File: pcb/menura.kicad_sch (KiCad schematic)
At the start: 53 parts, among them SW1 SW_Push, SW10 SW_Push, SW11 SW_Push, SW12 SW_Push, SW13 SW_Push, SW14 SW_Push, SW15 SW_Push, SW16 SW_Push, SW17 SW_Push, SW18 SW_Push, SW19 SW_Push, SW2 SW_Push, SW20 SW_Push, SW21 SW_Push, SW22 SW_Push, SW3 SW_Push, SW4 SW_Push, SW5 SW_Push, SW6 SW_Push, SW7 SW_Push, SW8 SW_Push, SW9 SW_Push

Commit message: fix diode ordering
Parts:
- renumbered D20 to D19, D22 to D20, D19 to D21, D21 to D22, SW20 to SW19, SW22 to SW20, SW19 to SW21, SW21 to SW22
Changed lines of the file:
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@@
 		(on_board yes)
 		(dnp no)
-		(property "Reference" "D19"
+		(property "Reference" "D21"
 			(at 154.94 105.41 90)
 			(effects
@@
 			(project "menura"
 				(path "/e9ea61dd-32b8-44c9-bab5-2f724da397cf"
-					(reference "D19")
+					(reference "D21")
 					(unit 1)
 				)
@@
 		(on_board yes)
 		(dnp no)
-		(property "Reference" "D22"
+		(property "Reference" "D20"
 			(at 179.07 91.44 90)
 			(effects
@@
 			(project "menura"
 				(path "/e9ea61dd-32b8-44c9-bab5-2f724da397cf"
-					(reference "D22")
+					(reference "D20")
 					(unit 1)
 				)
@@
 		(on_board yes)
 		(dnp no)
-		(property "Reference" "SW22"
+		(property "Reference" "SW20"
 			(at 170.18 82.55 0)
 			(effects
@@
 			(project "menura"
 				(path "/e9ea61dd-32b8-44c9-bab5-2f724da397cf"
-					(reference "SW22")
+					(reference "SW20")
 					(unit 1)
 				)
@@
 		(on_board yes)
 		(dnp no)
-		(property "Reference" "D20"
+		(property "Reference" "D19"
 			(at 160.02 91.44 90)
 			(effects
@@
 			(project "menura"
 				(path "/e9ea61dd-32b8-44c9-bab5-2f724da397cf"
-					(reference "D20")
+					(reference "D19")
 					(unit 1)
 				)
@@
 		(on_board yes)
 		(dnp no)
-		(property "Reference" "SW19"
+		(property "Reference" "SW21"
 			(at 146.05 96.52 0)
 			(effects
@@
 			(project "menura"
 				(path "/e9ea61dd-32b8-44c9-bab5-2f724da397cf"
-					(reference "SW19")
+					(reference "SW21")
 					(unit 1)
 				)
@@
 		(on_board yes)
 		(dnp no)
-		(property "Reference" "SW20"
+		(property "Reference" "SW19"
 			(at 151.13 82.55 0)
 			(effects
@@
 			(project "menura"
 				(path "/e9ea61dd-32b8-44c9-bab5-2f724da397cf"
-					(reference "SW20")
+					(reference "SW19")
 					(unit 1)
 				)
@@
 		(on_board yes)
 		(dnp no)
-		(property "Reference" "D21"
+		(property "Reference" "D22"
 			(at 173.99 105.41 90)
 			(effects
@@
 			(project "menura"
 				(path "/e9ea61dd-32b8-44c9-bab5-2f724da397cf"
-					(reference "D21")
+					(reference "D22")
 					(unit 1)
 				)
@@
 		(on_board yes)
 		(dnp no)
-		(property "Reference" "SW21"
+		(property "Reference" "SW22"
 			(at 165.1 96.52 0)
 			(effects
@@
 			(project "menura"
 				(path "/e9ea61dd-32b8-44c9-bab5-2f724da397cf"
-					(reference "SW21")
+					(reference "SW22")
 					(unit 1)
 				)

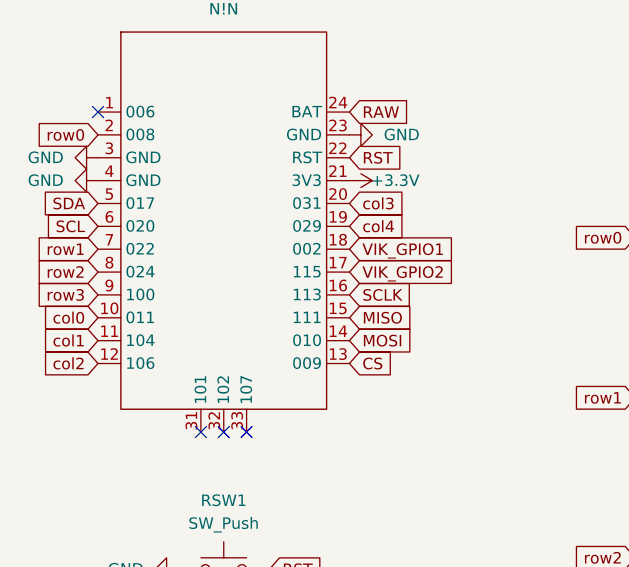
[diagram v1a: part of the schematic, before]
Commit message: fix: spi pins should be high freq
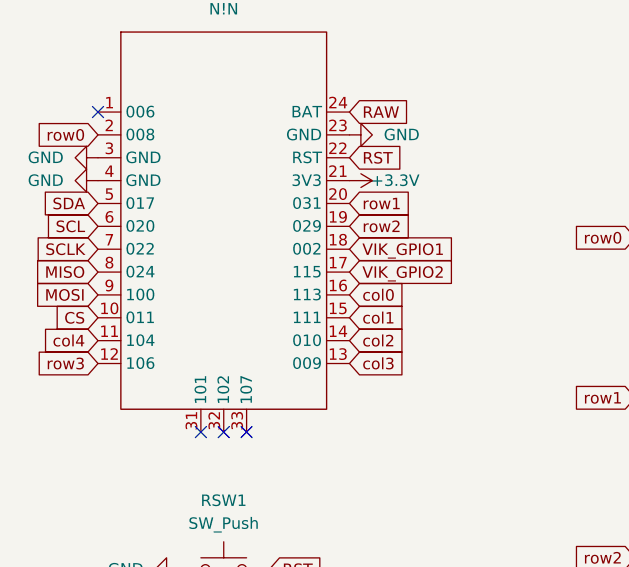
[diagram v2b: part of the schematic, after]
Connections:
- net CS: now also MCU1.10 (011); no longer MCU1.13 (009)
- net MISO: now also MCU1.8 (024); no longer MCU1.15 (111)
- net MOSI: now also MCU1.9 (100); no longer MCU1.14 (010)
- net SCLK: now also MCU1.7 (022); no longer MCU1.16 (113)
- net col0: now also MCU1.16 (113); no longer MCU1.10 (011)
- net col1: now also MCU1.15 (111); no longer MCU1.11 (104)
- net col2: now also MCU1.14 (010); no longer MCU1.12 (106)
- net col3: now also MCU1.13 (009); no longer MCU1.20 (031)
- net col4: now also MCU1.11 (104); no longer MCU1.19 (029)
- net row1: now also MCU1.20 (031); no longer MCU1.7 (022)
- net row2: now also MCU1.19 (029); no longer MCU1.8 (024)
- net row3: now also MCU1.12 (106); no longer MCU1.9 (100)

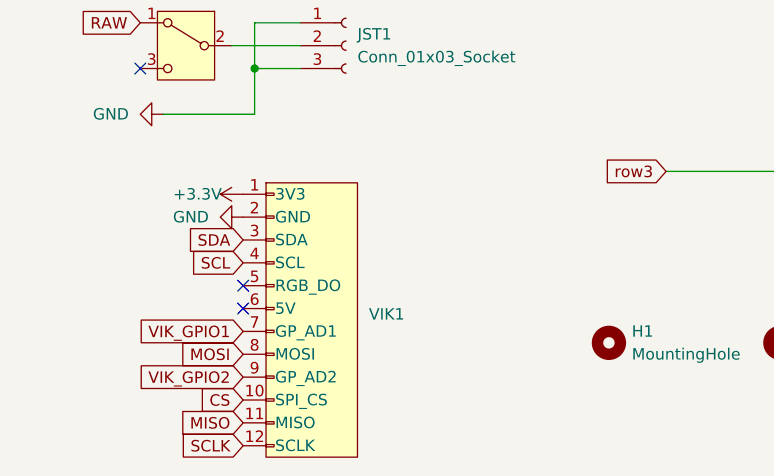
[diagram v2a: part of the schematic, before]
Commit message: add vik throughole breakout
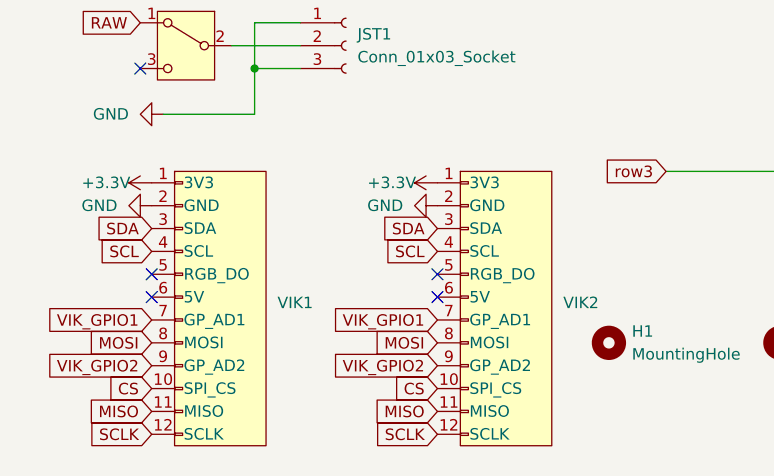
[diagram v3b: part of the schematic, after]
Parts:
- added VIK2: ~, quappo:Connector_vik-keyboard-throughhole, symbol _quappo:vik-keyboard-connector
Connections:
- net +3.3V: now also VIK2.1 (3V3)
- net CS: now also VIK2.10 (SPI_CS)
- net GND: now also VIK2.2 (GND)
- net MISO: now also VIK2.11 (MISO)
- net MOSI: now also VIK2.8 (MOSI)
- net SCL: now also VIK2.4 (SCL)
- net SCLK: now also VIK2.12 (SCLK)
- net SDA: now also VIK2.3 (SDA)
- net VIK_GPIO1: now also VIK2.7 (GP_AD1)
- net VIK_GPIO2: now also VIK2.9 (GP_AD2)
- no-connect marks 7 -> 9
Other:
- moved on the sheet: VIK1

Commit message: logo silkscreens
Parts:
- added LOGO1: menura, quappo:Logo_menura, symbol Graphic:Logo_Open_Hardware_Small
- added LOGO2: vik, quappo:Logo_vik-small, symbol Graphic:Logo_Open_Hardware_Small
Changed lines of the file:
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@@
+	)
+	(symbol
+		(lib_id "Graphic:Logo_Open_Hardware_Small")
+		(at 83.82 144.78 0)
+		(unit 1)
+		(exclude_from_sim yes)
+		(in_bom no)
+		(on_board yes)
+		(dnp no)
+		(fields_autoplaced yes)
+		(property "Reference" "LOGO1"
+			(at 90.17 142.8749 0)
+			(effects
+				(font
+					(size 1.27 1.27)
+				)
+				(justify left)
+			)
+		)
+		(property "Value" "menura"
+			(at 90.17 145.4149 0)
+			(effects
+				(font
+					(size 1.27 1.27)
+				)
+				(justify left)
+			)
+		)
+		(property "Footprint" "quappo:Logo_menura"
+			(at 83.82 144.78 0)
+			(effects
+				(font
+					(size 1.27 1.27)
+				)
+				(hide yes)
+			)
+		)
+		(property "Datasheet" "~"
+			(at 83.82 144.78 0)
+			(effects
+				(font
+					(size 1.27 1.27)
+				)
+				(hide yes)
+			)
+		)
+		(property "Description" "Open Hardware logo, small"
+			(at 83.82 144.78 0)
+			(effects
+				(font
+					(size 1.27 1.27)
+				)
+				(hide yes)
+			)
+		)
+		(property "Sim.Enable" "0"
+			(at 83.82 144.78 0)
+			(effects
+				(font
+					(size 1.27 1.27)
+				)
+				(hide yes)
+			)
+		)
+		(instances
+			(project "menura"
+				(path "/e9ea61dd-32b8-44c9-bab5-2f724da397cf"
+					(reference "LOGO1")
+					(unit 1)
+				)
+			)
+		)
 	)
 	(symbol
@@
 					(unit 1)
 				)
+			)
+		)
+	)
+	(symbol
+		(lib_id "Graphic:Logo_Open_Hardware_Small")
+		(at 109.22 144.78 0)
+		(unit 1)
+		(exclude_from_sim yes)
+		(in_bom no)
+		(on_board yes)
+		(dnp no)
+		(fields_autoplaced yes)
+		(property "Reference" "LOGO2"
+			(at 115.57 142.8749 0)
+			(effects
+				(font
+					(size 1.27 1.27)
+				)
+				(justify left)
+			)
+		)
+		(property "Value" "vik"
+			(at 115.57 145.4149 0)
+			(effects
+				(font
+					(size 1.27 1.27)
+				)
+				(justify left)
+			)
+		)
+		(property "Footprint" "quappo:Logo_vik-small"
+			(at 109.22 144.78 0)
+			(effects
+				(font
+					(size 1.27 1.27)
+				)
+				(hide yes)
+			)
+		)
+		(property "Datasheet" "~"
+			(at 109.22 144.78 0)
+			(effects
+				(font
+					(size 1.27 1.27)
+				)
+				(hide yes)
+			)
+		)
+		(property "Description" "Open Hardware logo, small"
+			(at 109.22 144.78 0)
+			(effects
+				(font
+					(size 1.27 1.27)
+				)
+				(hide yes)
+			)
+		)
+		(property "Sim.Enable" "0"
+			(at 109.22 144.78 0)
+			(effects
+				(font
+					(size 1.27 1.27)
+				)
+				(hide yes)
+			)
+		)
+		(instances
+			(project "menura"
+				(path "/e9ea61dd-32b8-44c9-bab5-2f724da397cf"
+					(reference "LOGO2")
+					(unit 1)
+				)

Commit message: holes
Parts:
- added PH1, PH2: MountingHole, symbol Mechanical:MountingHole
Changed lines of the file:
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@@
+	)
+	(symbol
+		(lib_id "Mechanical:MountingHole")
+		(at 105.41 158.75 0)
+		(unit 1)
+		(exclude_from_sim yes)
+		(in_bom no)
+		(on_board yes)
+		(dnp no)
+		(fields_autoplaced yes)
+		(property "Reference" "PH2"
+			(at 107.95 157.4799 0)
+			(effects
+				(font
+					(size 1.27 1.27)
+				)
+				(justify left)
+			)
+		)
+		(property "Value" "MountingHole"
+			(at 107.95 160.0199 0)
+			(effects
+				(font
+					(size 1.27 1.27)
+				)
+				(justify left)
+			)
+		)
+		(property "Footprint" ""
+			(at 105.41 158.75 0)
+			(effects
+				(font
+					(size 1.27 1.27)
+				)
+				(hide yes)
+			)
+		)
+		(property "Datasheet" "~"
+			(at 105.41 158.75 0)
+			(effects
+				(font
+					(size 1.27 1.27)
+				)
+				(hide yes)
+			)
+		)
+		(property "Description" "Mounting Hole without connection"
+			(at 105.41 158.75 0)
+			(effects
+				(font
+					(size 1.27 1.27)
+				)
+				(hide yes)
+			)
+		)
+		(instances
+			(project "menura"
+				(path "/e9ea61dd-32b8-44c9-bab5-2f724da397cf"
+					(reference "PH2")
+					(unit 1)
+				)
+			)
+		)
 	)
 	(symbol
@@
 	)
 	(symbol
+		(lib_id "Mechanical:MountingHole")
+		(at 82.55 158.75 0)
+		(unit 1)
+		(exclude_from_sim yes)
+		(in_bom no)
+		(on_board yes)
+		(dnp no)
+		(fields_autoplaced yes)
+		(property "Reference" "PH1"
+			(at 85.09 157.4799 0)
+			(effects
+				(font
+					(size 1.27 1.27)
+				)
+				(justify left)
+			)
+		)
+		(property "Value" "MountingHole"
+			(at 85.09 160.0199 0)
+			(effects
+				(font
+					(size 1.27 1.27)
+				)
+				(justify left)
+			)
+		)
+		(property "Footprint" ""
+			(at 82.55 158.75 0)
+			(effects
+				(font
+					(size 1.27 1.27)
+				)
+				(hide yes)
+			)
+		)
+		(property "Datasheet" "~"
+			(at 82.55 158.75 0)
+			(effects
+				(font
+					(size 1.27 1.27)
+				)
+				(hide yes)
+			)
+		)
+		(property "Description" "Mounting Hole without connection"
+			(at 82.55 158.75 0)
+			(effects
+				(font
+					(size 1.27 1.27)
+				)
+				(hide yes)
+			)
+		)
+		(instances
+			(project "menura"
+				(path "/e9ea61dd-32b8-44c9-bab5-2f724da397cf"
+					(reference "PH1")
+					(unit 1)
+				)
+			)
+		)
+	)
+	(symbol
 		(lib_id "Diode:1N4148W")
 		(at 99.06 40.64 90)
@@
 			)
 		)
-		(property "Sim.Enable" "0"
-			(at 83.82 144.78 0)
-			(effects
-				(font
-					(size 1.27 1.27)
-				)
-				(hide yes)
-			)
-		)
 		(instances
 			(project "menura"
@@
 			(at 109.22 144.78 0)
 			(effects
-				(font
-					(size 1.27 1.27)
-				)
-				(hide yes)
-			)
-		)
-		(property "Sim.Enable" "0"
-			(at 109.22 144.78 0)
-			(effects

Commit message: one more pth
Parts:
- added PH3: MountingHole, MountingHole:MountingHole_2.2mm_M2_Pad, symbol Mechanical:MountingHole
- PH1, PH2: footprint (none) -> MountingHole:MountingHole_2.2mm_M2_Pad
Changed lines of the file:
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@@
+	)
+	(symbol
+		(lib_id "Mechanical:MountingHole")
+		(at 125.73 158.75 0)
+		(unit 1)
+		(exclude_from_sim yes)
+		(in_bom no)
+		(on_board yes)
+		(dnp no)
+		(fields_autoplaced yes)
+		(property "Reference" "PH3"
+			(at 128.27 157.4799 0)
+			(effects
+				(font
+					(size 1.27 1.27)
+				)
+				(justify left)
+			)
+		)
+		(property "Value" "MountingHole"
+			(at 128.27 160.0199 0)
+			(effects
+				(font
+					(size 1.27 1.27)
+				)
+				(justify left)
+			)
+		)
+		(property "Footprint" "MountingHole:MountingHole_2.2mm_M2_Pad"
+			(at 125.73 158.75 0)
+			(effects
+				(font
+					(size 1.27 1.27)
+				)
+				(hide yes)
+			)
+		)
+		(property "Datasheet" "~"
+			(at 125.73 158.75 0)
+			(effects
+				(font
+					(size 1.27 1.27)
+				)
+				(hide yes)
+			)
+		)
+		(property "Description" "Mounting Hole without connection"
+			(at 125.73 158.75 0)
+			(effects
+				(font
+					(size 1.27 1.27)
+				)
+				(hide yes)
+			)
+		)
+		(instances
+			(project "menura"
+				(path "/e9ea61dd-32b8-44c9-bab5-2f724da397cf"
+					(reference "PH3")
+					(unit 1)
+				)
+			)
+		)
 	)
 	(symbol
@@
 			)
 		)
-		(property "Footprint" ""
+		(property "Footprint" "MountingHole:MountingHole_2.2mm_M2_Pad"
 			(at 105.41 158.75 0)
 			(effects
@@
 			)
 		)
-		(property "Footprint" ""
+		(property "Footprint" "MountingHole:MountingHole_2.2mm_M2_Pad"
 			(at 82.55 158.75 0)
 			(effects

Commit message: remove plated holes on inner edge
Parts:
- removed PH1, PH2, PH3: MountingHole, MountingHole:MountingHole_2.2mm_M2_Pad, symbol Mechanical:MountingHole
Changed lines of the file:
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@@
-	)
-	(symbol
-		(lib_id "Mechanical:MountingHole")
-		(at 125.73 158.75 0)
-		(unit 1)
-		(exclude_from_sim yes)
-		(in_bom no)
-		(on_board yes)
-		(dnp no)
-		(fields_autoplaced yes)
-		(property "Reference" "PH3"
-			(at 128.27 157.4799 0)
-			(effects
-				(font
-					(size 1.27 1.27)
-				)
-				(justify left)
-			)
-		)
-		(property "Value" "MountingHole"
-			(at 128.27 160.0199 0)
-			(effects
-				(font
-					(size 1.27 1.27)
-				)
-				(justify left)
-			)
-		)
-		(property "Footprint" "MountingHole:MountingHole_2.2mm_M2_Pad"
-			(at 125.73 158.75 0)
-			(effects
-				(font
-					(size 1.27 1.27)
-				)
-				(hide yes)
-			)
-		)
-		(property "Datasheet" "~"
-			(at 125.73 158.75 0)
-			(effects
-				(font
-					(size 1.27 1.27)
-				)
-				(hide yes)
-			)
-		)
-		(property "Description" "Mounting Hole without connection"
-			(at 125.73 158.75 0)
-			(effects
-				(font
-					(size 1.27 1.27)
-				)
-				(hide yes)
-			)
-		)
-		(instances
-			(project "menura"
-				(path "/e9ea61dd-32b8-44c9-bab5-2f724da397cf"
-					(reference "PH3")
-					(unit 1)
-				)
-			)
-		)
 	)
 	(symbol
@@
 	)
 	(symbol
-		(lib_id "Mechanical:MountingHole")
-		(at 105.41 158.75 0)
-		(unit 1)
-		(exclude_from_sim yes)
-		(in_bom no)
-		(on_board yes)
-		(dnp no)
-		(fields_autoplaced yes)
-		(property "Reference" "PH2"
-			(at 107.95 157.4799 0)
-			(effects
-				(font
-					(size 1.27 1.27)
-				)
-				(justify left)
-			)
-		)
-		(property "Value" "MountingHole"
-			(at 107.95 160.0199 0)
-			(effects
-				(font
-					(size 1.27 1.27)
-				)
-				(justify left)
-			)
-		)
-		(property "Footprint" "MountingHole:MountingHole_2.2mm_M2_Pad"
-			(at 105.41 158.75 0)
-			(effects
-				(font
-					(size 1.27 1.27)
-				)
-				(hide yes)
-			)
-		)
-		(property "Datasheet" "~"
-			(at 105.41 158.75 0)
-			(effects
-				(font
-					(size 1.27 1.27)
-				)
-				(hide yes)
-			)
-		)
-		(property "Description" "Mounting Hole without connection"
-			(at 105.41 158.75 0)
-			(effects
-				(font
-					(size 1.27 1.27)
-				)
-				(hide yes)
-			)
-		)
-		(instances
-			(project "menura"
-				(path "/e9ea61dd-32b8-44c9-bab5-2f724da397cf"
-					(reference "PH2")
-					(unit 1)
-				)
-			)
-		)
-	)
-	(symbol
 		(lib_id "power:GND")
 		(at 33.02 81.28 270)
@@
 					(unit 1)
 				)
-			)
-		)
-	)
-	(symbol
-		(lib_id "Mechanical:MountingHole")
-		(at 82.55 158.75 0)
-		(unit 1)
-		(exclude_from_sim yes)
-		(in_bom no)
-		(on_board yes)
-		(dnp no)
-		(fields_autoplaced yes)
-		(property "Reference" "PH1"
-			(at 85.09 157.4799 0)
-			(effects
-				(font
-					(size 1.27 1.27)
-				)
-				(justify left)
-			)
-		)
-		(property "Value" "MountingHole"
-			(at 85.09 160.0199 0)
-			(effects
-				(font
-					(size 1.27 1.27)
-				)
-				(justify left)
-			)
-		)
-		(property "Footprint" "MountingHole:MountingHole_2.2mm_M2_Pad"
-			(at 82.55 158.75 0)
-			(effects
-				(font
-					(size 1.27 1.27)
-				)
-				(hide yes)
-			)
-		)
-		(property "Datasheet" "~"
-			(at 82.55 158.75 0)
-			(effects
-				(font
-					(size 1.27 1.27)
-				)
-				(hide yes)
-			)
-		)
-		(property "Description" "Mounting Hole without connection"
-			(at 82.55 158.75 0)
-			(effects
-				(font
-					(size 1.27 1.27)
-				)
-				(hide yes)
-			)
-		)
-		(instances
-			(project "menura"
-				(path "/e9ea61dd-32b8-44c9-bab5-2f724da397cf"
-					(reference "PH1")
-					(unit 1)
-				)

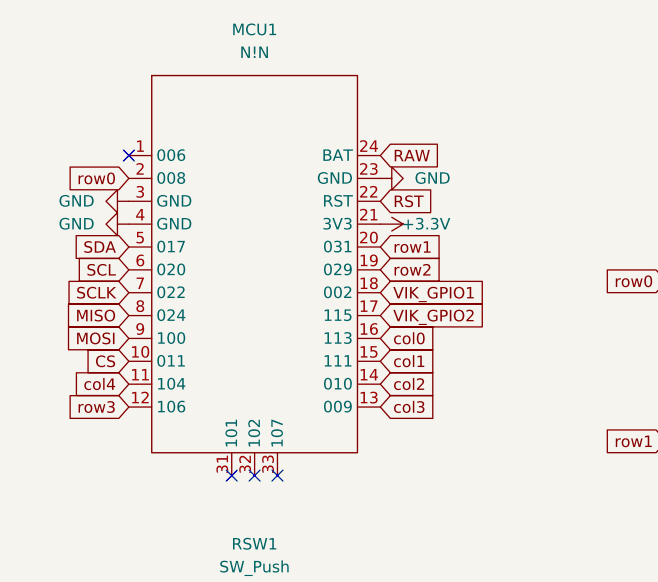
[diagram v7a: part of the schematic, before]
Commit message: reorder a few pins
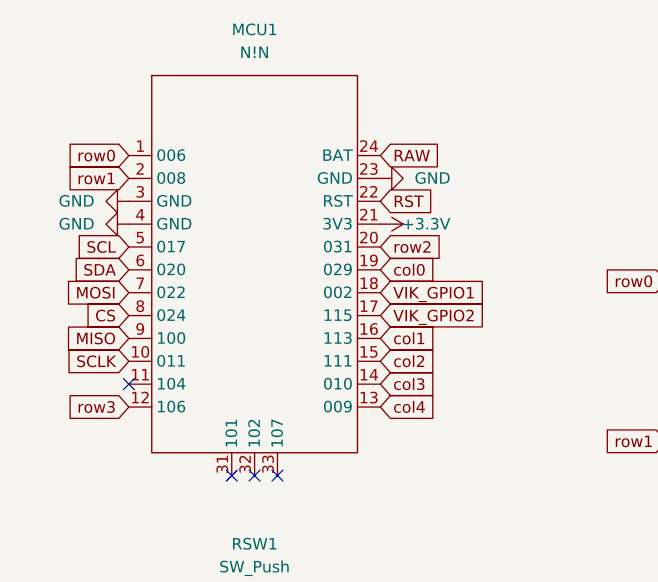
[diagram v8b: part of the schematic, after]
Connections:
- net CS: now also MCU1.8 (024); no longer MCU1.10 (011)
- net MISO: now also MCU1.9 (100); no longer MCU1.8 (024)
- net MOSI: now also MCU1.7 (022); no longer MCU1.9 (100)
- net SCL: now also MCU1.5 (017); no longer MCU1.6 (020)
- net SCLK: now also MCU1.10 (011); no longer MCU1.7 (022)
- net SDA: now also MCU1.6 (020); no longer MCU1.5 (017)
- net col0: now also MCU1.19 (029); no longer MCU1.16 (113)
- net col1: now also MCU1.16 (113); no longer MCU1.15 (111)
- net col2: now also MCU1.15 (111); no longer MCU1.14 (010)
- net col3: now also MCU1.14 (010); no longer MCU1.13 (009)
- net col4: now also MCU1.13 (009); no longer MCU1.11 (104)
- net row0: now also MCU1.1 (006); no longer MCU1.2 (008)
- net row1: now also MCU1.2 (008); no longer MCU1.20 (031)
- net row2: now also MCU1.20 (031); no longer MCU1.19 (029)
